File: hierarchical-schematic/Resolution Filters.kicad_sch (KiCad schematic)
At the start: 25 parts, among them J501 Conn_Coaxial, J502 Conn_Coaxial

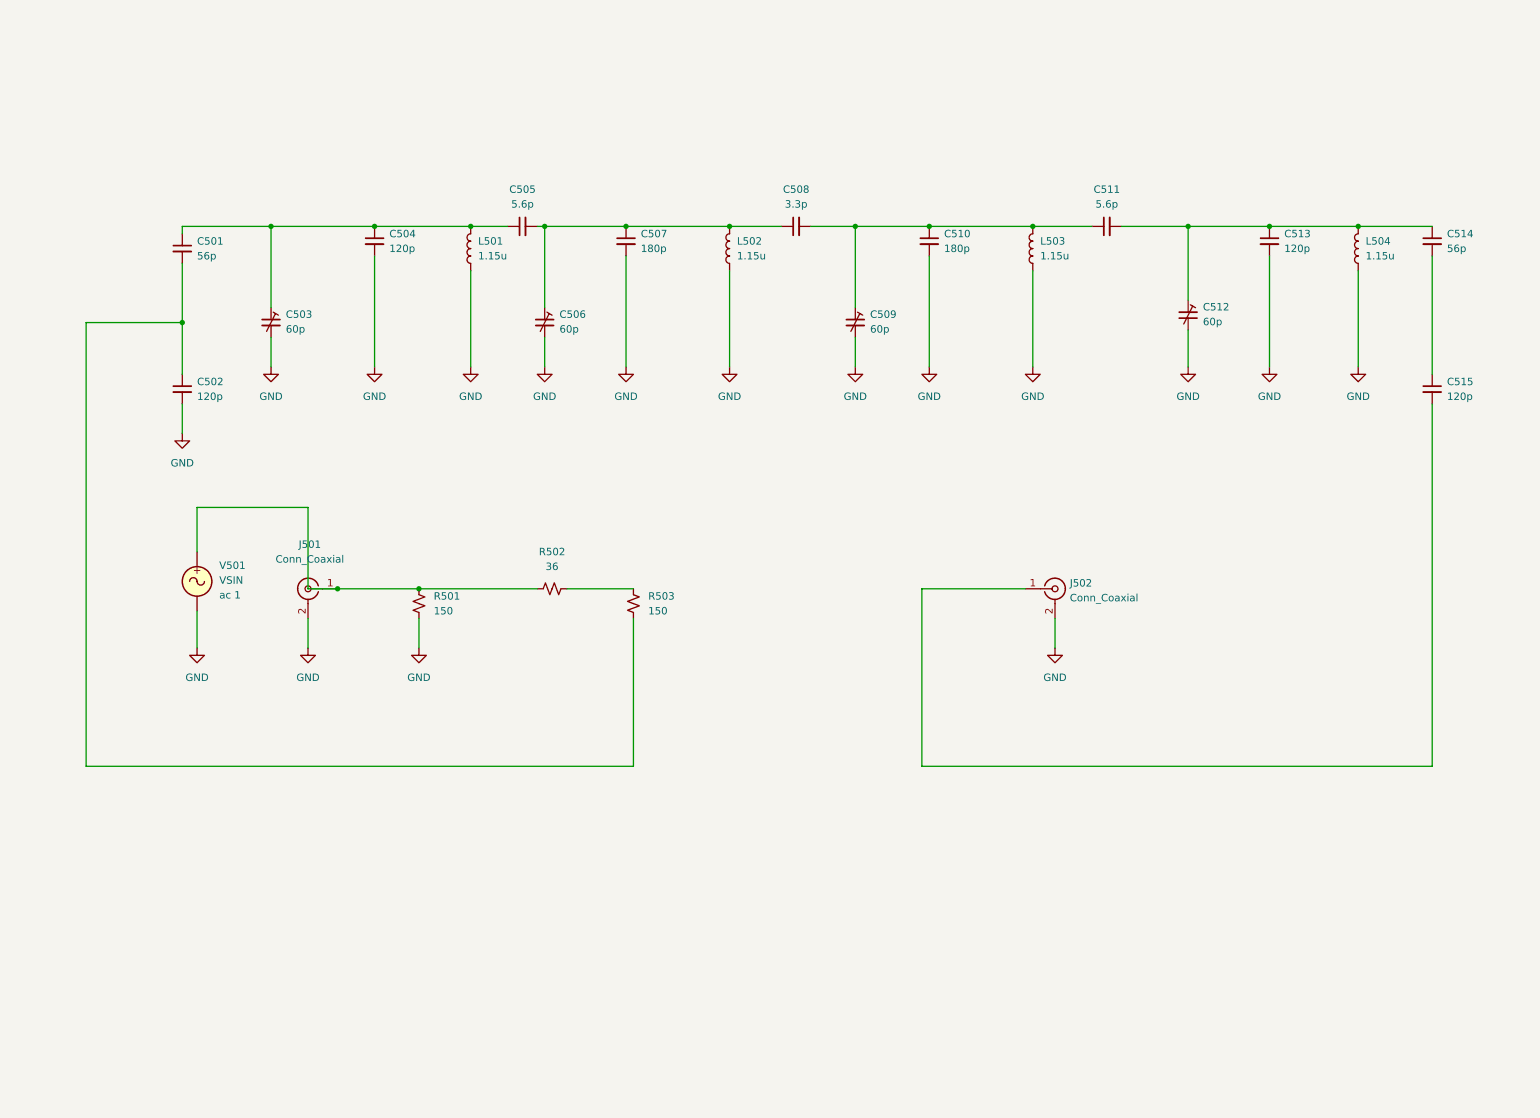
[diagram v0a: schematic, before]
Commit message: 15v-supply changes
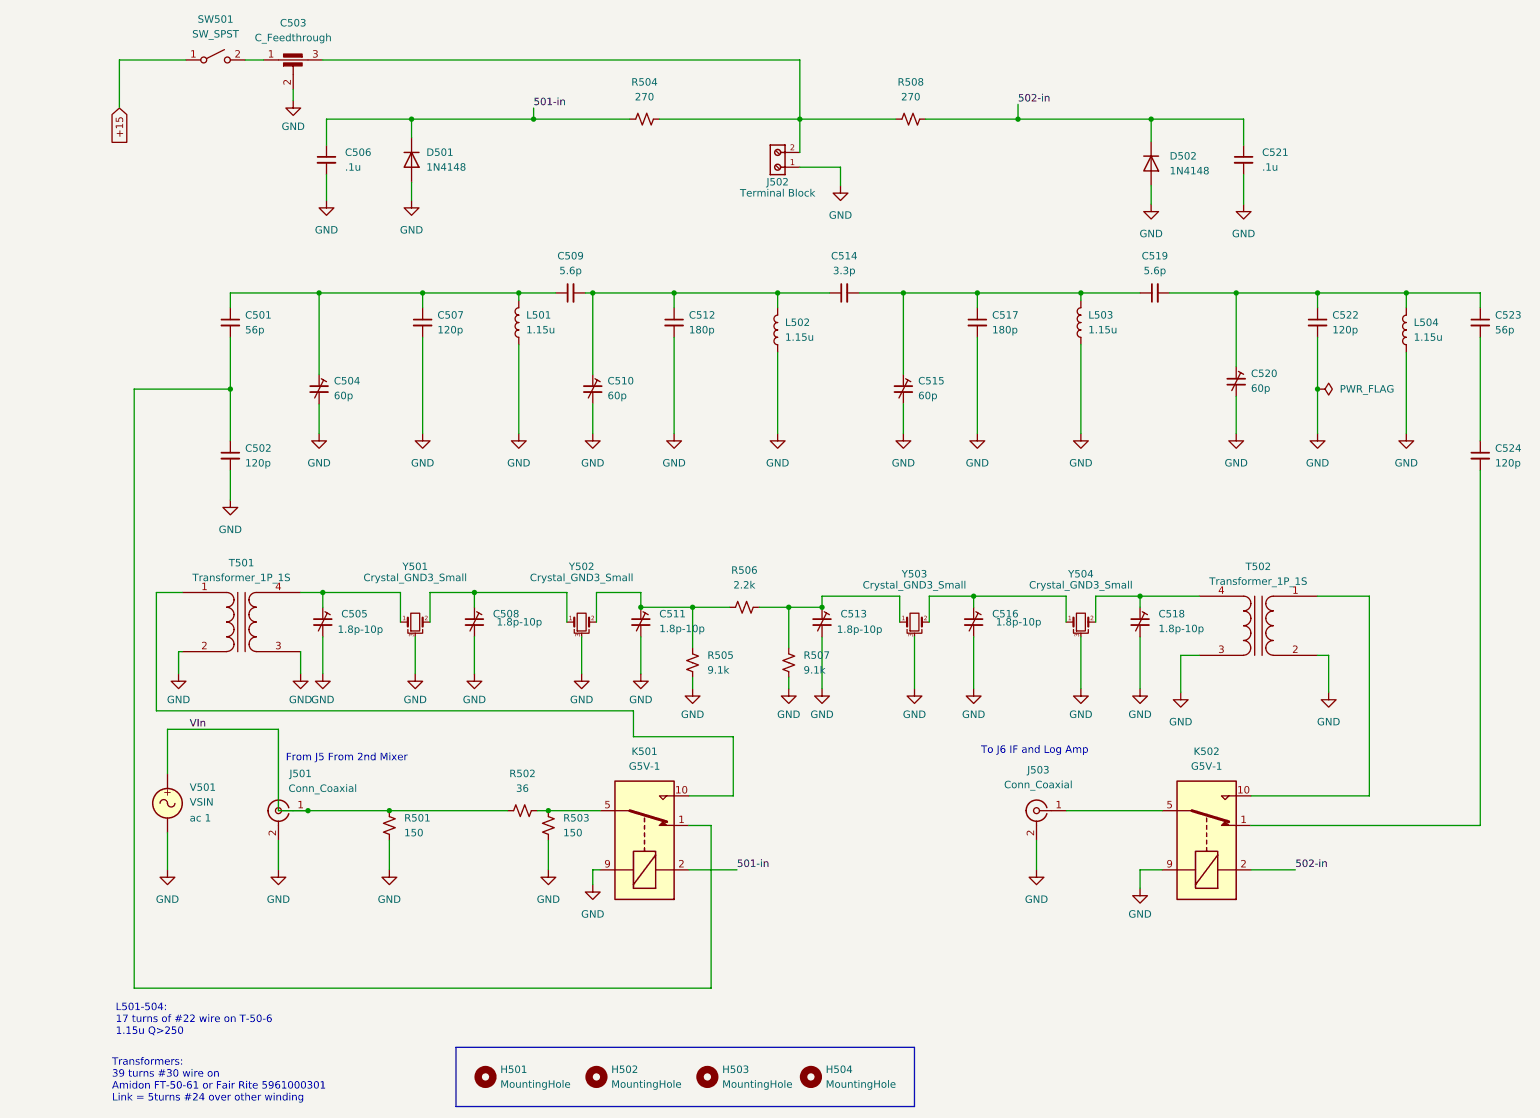
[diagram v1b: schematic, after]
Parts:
- removed C503, C506, C509, C512: 60p, symbol Device:C_Trim_Small
- removed C504, C513, C515: 120p, symbol Device:C_Small
- removed C505, C511: 5.6p, symbol Device:C_Small
- removed C508: 3.3p, symbol Device:C_Small
- removed C510: 180p, symbol Device:C_Small
- removed J502: Conn_Coaxial, symbol Connector:Conn_Coaxial
- added C503: C_Feedthrough, symbol Device:C_Feedthrough
- added C504, C510, C515: 60p, resolution-filters:GKG60015, symbol Device:C_Trim_Small
- added C505, C508, C511, C513, C516, C518: 1.8p-10p, symbol Device:C_Trim_Small
- added C506, C521: .1u, Capacitor_THT:C_Radial_D4.0mm_H5.0mm_P1.50mm, symbol Device:C_Small
- added C509, C519: 5.6p, Capacitor_THT:C_Radial_D4.0mm_H5.0mm_P1.50mm, symbol Device:C_Small
- added C512, C517: 180p, Capacitor_THT:C_Radial_D4.0mm_H5.0mm_P1.50mm, symbol Device:C_Small
- added C520: 60p, Capacitor_THT:C_Radial_D4.0mm_H5.0mm_P1.50mm, symbol Device:C_Trim_Small
- added C522, C524: 120p, Capacitor_THT:C_Radial_D4.0mm_H5.0mm_P1.50mm, symbol Device:C_Small
- added C523: 56p, Capacitor_THT:C_Radial_D4.0mm_H5.0mm_P1.50mm, symbol Device:C_Small
- added D501, D502: 1N4148, Diode_THT:D_DO-35_SOD27_P7.62mm_Horizontal, symbol Diode:1N4148
- added H501, H502, H503, H504: MountingHole, MountingHole:MountingHole_3.2mm_M3, symbol Mechanical:MountingHole
- added J502: Terminal Block, resolution-filters:691137710002, symbol 691137710002:691137710002
- added J503: Conn_Coaxial, resolution-filters:XTAL_ECS-10.7-7.5B, symbol Connector:Conn_Coaxial
- added K501, K502: G5V-1, Relay_THT:Relay_SPDT_Omron_G5V-1, symbol Relay:G5V-1
- added R504, R508: 270, Resistor_THT:R_Axial_DIN0207_L6.3mm_D2.5mm_P7.62mm_Horizontal, symbol Device:R_Small_US
- added R505, R507: 9.1k, Resistor_THT:R_Axial_DIN0207_L6.3mm_D2.5mm_P7.62mm_Horizontal, symbol Device:R_Small_US
- added R506: 2.2k, Resistor_THT:R_Axial_DIN0207_L6.3mm_D2.5mm_P7.62mm_Horizontal, symbol Device:R_Small_US
- added SW501: SW_SPST, symbol Switch:SW_SPST
- added T501, T502: Transformer_1P_1S, Inductor_THT:L_Toroid_Vertical_L13.0mm_W6.5mm_P5.60mm, symbol Device:Transformer_1P_1S
- added Y501, Y502, Y503, Y504: Crystal_GND3_Small, resolution-filters:XTAL_ECS-10.7-7.5B, symbol Device:Crystal_GND3_Small
- C501, C502: footprint (none) -> Capacitor_THT:C_Radial_D4.0mm_H5.0mm_P1.50mm
- C507: value 180p -> 120p; footprint (none) -> Capacitor_THT:C_Radial_D4.0mm_H5.0mm_P1.50mm
- C514: value 56p -> 3.3p; footprint (none) -> Capacitor_THT:C_Radial_D4.0mm_H5.0mm_P1.50mm
- J501: footprint (none) -> resolution-filters:XTAL_ECS-10.7-7.5B; Spice_Model (none) -> Conn_Coaxial; Spice_Netlist_Enabled (none) -> N; Spice_Primitive (none) -> J
- L501, L502, L503, L504: footprint (none) -> Inductor_THT:L_Toroid_Vertical_L13.0mm_W6.5mm_P5.60mm
- R501, R502, R503: footprint (none) -> Resistor_THT:R_Axial_DIN0207_L6.3mm_D2.5mm_P7.62mm_Horizontal
- V501: now left out of the parts list
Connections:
- net GND: now also R503.2, C503.2, C504.2, C505.2, C506.2, C508.2, C510.2, C511.2, C512.2, C513.2, C515.2, C516.2, C517.2, C518.2, C520.2, C521.2, C522.2, D501.2 (A), D502.2 (A), J502.1, J503.2 (Ext), K501.9, K502.9, R505.2, R507.2, T501.2 (AB), T501.3 (SA), T502.2 (AB), T502.3 (SA), Y501.3, Y502.3, Y503.3, Y504.3
- net VIn: now reaches J501.1 (In), R501.1, R502.1, V501.1
- net at L503.1: now also C514.2, C515.1, C517.1, C519.1
- net at C507.1: now also C501.1, L501.1, C504.1, C509.1; no longer L502.1
- net at L504.1: now also C519.2, C520.1, C522.1, C523.1; no longer C514.1
- net at R502.2, R503.1: now also K501.5, K501.6
- net at C501.2, C502.1: now also K501.1; no longer R503.2
- new net: C503.3, J502.2, R504.2, R508.1
- new net: K501.10, T501.1 (AA)
- new net: C505.1, T501.4 (SB), Y501.1
- new net: C513.1, R506.2, R507.1, Y503.1
- new net: C508.1, Y501.2, Y502.1
- new net: C503.1, SW501.2 (B)
- new net: C511.1, R505.1, R506.1, Y502.2
- new net: C518.1, T502.4 (SB), Y504.2
- new net: C509.2, C510.1, C512.1, C514.1, L502.1
- new net: J503.1 (In), K502.5, K502.6
- new net: K502.10, T502.1 (AA)
- new net: C516.1, Y503.2, Y504.1
- new net: C523.2, C524.1
- new net: C524.2, K502.1
- new net +15: SW501.1 (A)
- new net 501-in: C506.1, D501.1 (K), K501.2, R504.1
- new net 502-in: C521.1, D502.1 (K), K502.2, R508.2
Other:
- note added: "From J5 From 2nd Mixer"
- note added: "L501-504: 17 turns of #22 wire on T-50-6 1.15u Q>250"
- note added: "To J6 IF and Log Amp"
- note added: "Transformers: 39 turns #30 wire on Amidon FT-50-61 or Fair Rite 5961000301 Link = 5turns #24 over other winding"

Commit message: 2ndmixer-2ndlo
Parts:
- C501, C502, C506, C507, C509, C512, C514, C517, C519, C521, C522, C523, C524: footprint Capacitor_THT:C_Radial_D4.0mm_H5.0mm_P1.50mm -> Capacitor_THT:C_Disc_D5.0mm_W2.5mm_P5.00mm
- C503: value C_Feedthrough -> 5n
- C504, C510, C515: value 60p -> 12p-60p
- C505, C508, C511, C513, C516, C518: footprint (none) -> resolution-filters:GKG60015
- C520: value 60p -> 12p-60p; footprint Capacitor_THT:C_Radial_D4.0mm_H5.0mm_P1.50mm -> resolution-filters:GKG60015
- J501, J503: footprint resolution-filters:XTAL_ECS-10.7-7.5B -> Connector_Wire:SolderWire-0.5sqmm_1x02_P4.6mm_D0.9mm_OD2.1mm
- T501, T502: footprint Inductor_THT:L_Toroid_Vertical_L13.0mm_W6.5mm_P5.60mm -> Transformer_THT:Transformer_Toroid_Horizontal_D14.0mm_Amidon-T50
- Y501, Y502, Y503, Y504: value Crystal_GND3_Small -> 10.7MHz
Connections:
- net +15 renamed +15 Regulated
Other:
- note added: ""@" indicates crystal orientation"
- note added: "@"

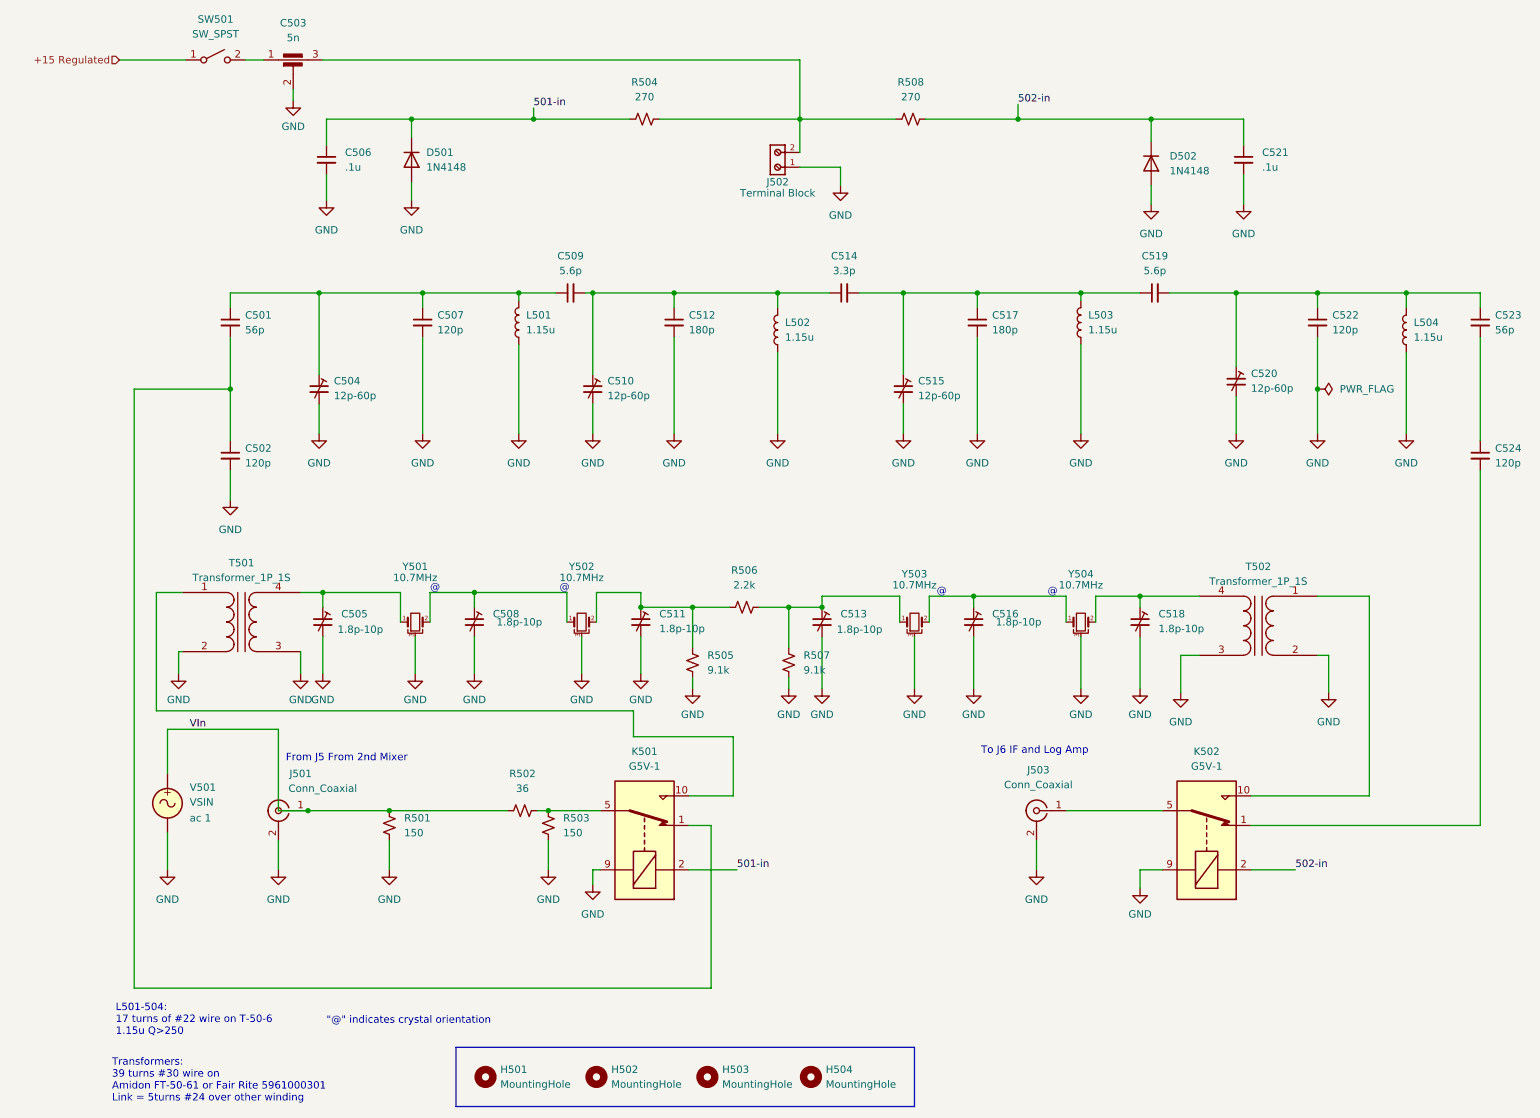
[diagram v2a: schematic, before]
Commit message: improved if and log amp and second lo/mixer
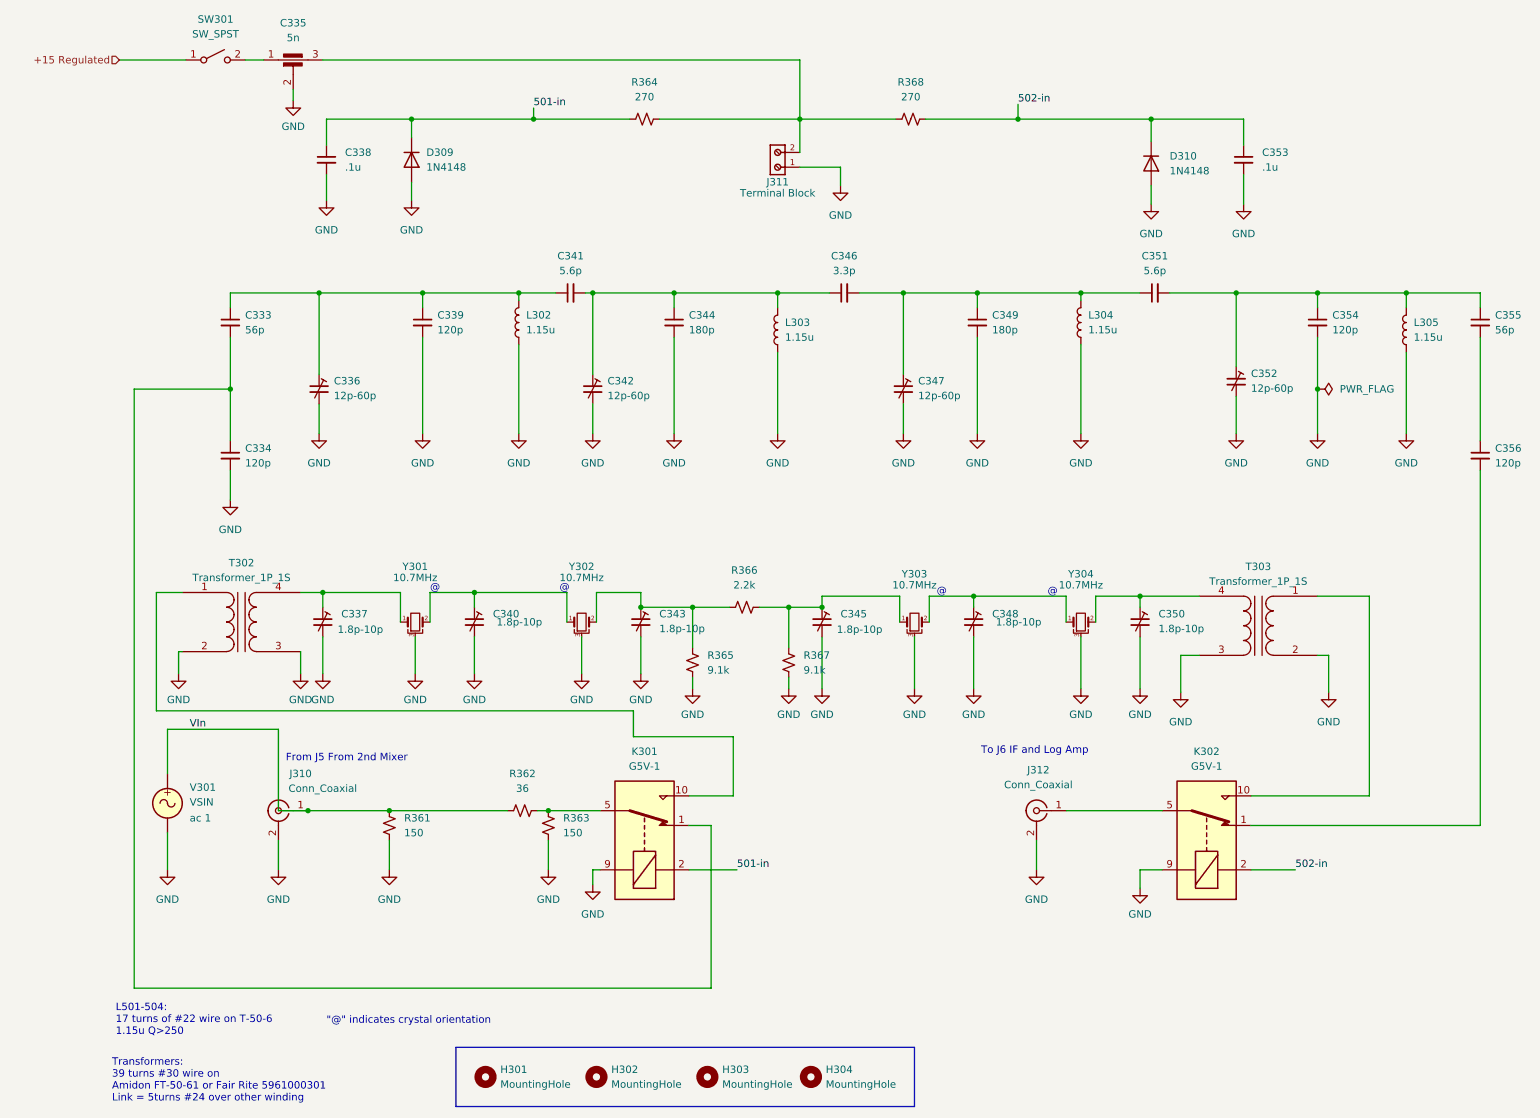
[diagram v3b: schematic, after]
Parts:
- renumbered C501 to C333, C502 to C334, C503 to C335, C504 to C336, C505 to C337, C506 to C338, C507 to C339, C508 to C340, C509 to C341, C510 to C342, C511 to C343, C512 to C344, C513 to C345, C514 to C346, C515 to C347, C516 to C348, C517 to C349, C518 to C350, C519 to C351, C520 to C352, C521 to C353, C522 to C354, C523 to C355, C524 to C356, D501 to D309, D502 to D310, H501 to H301, H502 to H302, H503 to H303, H504 to H304, J501 to J310, J502 to J311, J503 to J312, K501 to K301, K502 to K302, L501 to L302, L502 to L303, L503 to L304, L504 to L305, R501 to R361, R502 to R362, R503 to R363, R504 to R364, R505 to R365, R506 to R366, R507 to R367, R508 to R368, SW501 to SW301, T501 to T302, T502 to T303, V501 to V301, Y501 to Y301, Y502 to Y302, Y503 to Y303, Y504 to Y304
